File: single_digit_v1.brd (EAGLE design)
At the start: 101.6 x 50.8 mm, 85 parts

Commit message: ready for production
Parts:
- added R43, R44, R45: (no value), rcl:M0805
- added SL1: (no value), con-amp-quick:02P
- added T8, T9: (no value), transistor:SOT23-BEC
- T1, T2, T3, T4, T5, T6, T7: device transistor-neu-to92:TO92-EBC -> transistor:SOT23-BEC
- moved T2 9.17 mm to (83.8, 17.5), turned to 270 degrees
- moved R37 8.48 mm to (63.5, 36.8), turned to 135 degrees
- moved T3 7.44 mm to (69.5, 36.2), turned to 0 degrees
- moved T7 6.17 mm to (19.2, 16.0), turned to 180 degrees
- moved T4 5.88 mm to (73.0, 15.2), turned to 180 degrees
- moved R36 5.86 mm to (78.2, 18.5), turned to 180 degrees
- moved R41 4.73 mm to (25.8, 16.5)
- moved R42 4.59 mm to (16.0, 26.2)
- moved JP1 4.39 mm to (35.0, 25.0), turned to 270 degrees
- moved R39 4.05 mm to (62.8, 26.5)
- moved T1 3.83 mm to (15.0, 21.5), turned to 90 degrees
- moved T5 3.46 mm to (61.2, 21.5), turned to 90 degrees
- moved R38 3.38 mm to (67.8, 16.2)
- moved R40 2.23 mm to (28.2, 34.2)
- moved T6 2.21 mm to (22.8, 36.5), turned to 0 degrees
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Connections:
- new net N$50: R43.2, T8.C
- new net N$51: R43.1, R44.2, T9.B
- new net N$52: R45.1, T8.B
- new net N$53: R45.2, SL1.1
- new net VCC: LED1.A, LED10.A, LED11.A, LED12.A, LED13.A, LED14.A, LED15.A, LED16.A, LED17.A, LED18.A, LED19.A, LED2.A, LED20.A, LED21.A, LED22.A, LED23.A, LED24.A, LED25.A, LED26.A, LED27.A, LED28.A, LED29.A, LED3.A, LED30.A, LED31.A, LED32.A, LED33.A, LED34.A, LED35.A, LED4.A, LED5.A, LED6.A, LED7.A, LED8.A, LED9.A, T9.C
- net +5V: now also R44.1, SL1.2, T9.E; no longer JP1.5, LED1.A, LED10.A, LED11.A, LED12.A, LED13.A, LED14.A, LED15.A, LED16.A, LED17.A, LED18.A, LED19.A, LED2.A, LED20.A, LED21.A, LED22.A, LED23.A, LED24.A, LED25.A, LED26.A, LED27.A, LED28.A, LED29.A, LED3.A, LED30.A, LED31.A, LED32.A, LED33.A, LED34.A, LED35.A, LED4.A, LED5.A, LED6.A, LED7.A, LED8.A, LED9.A
- net GNDA: now also JP1.5, JP1.8, T8.E
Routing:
- net +5V: track 378.9 -> 16.7 mm
- net VCC: track 0.00 -> 55.7 mm, vias 0 -> 1
- net GNDA: track 0.00 -> 12.1 mm
- net S6: track 6.72 -> 18.4 mm
- net S7: track 22.6 -> 33.1 mm
- net N$51: track 0.00 -> 9.72 mm
- net S1: track 65.7 -> 74.7 mm, vias 2 -> 0
- net S5: track 6.72 -> 13.8 mm
- net N$50: track 0.00 -> 7.00 mm
- net S4: track 43.7 -> 50.6 mm
- net N$49: track 4.13 -> 9.31 mm
- net S3: track 48.0 -> 52.5 mm, vias 2 -> 0
- net N$53: track 0.00 -> 4.31 mm
- net N$52: track 0.00 -> 3.43 mm
- net N$42: track 4.13 -> 7.23 mm
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- added copper zone on layer 16, net VCC
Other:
- board size 101.6 x 50.8 mm -> 100 x 50 mm
- board text added: "+"

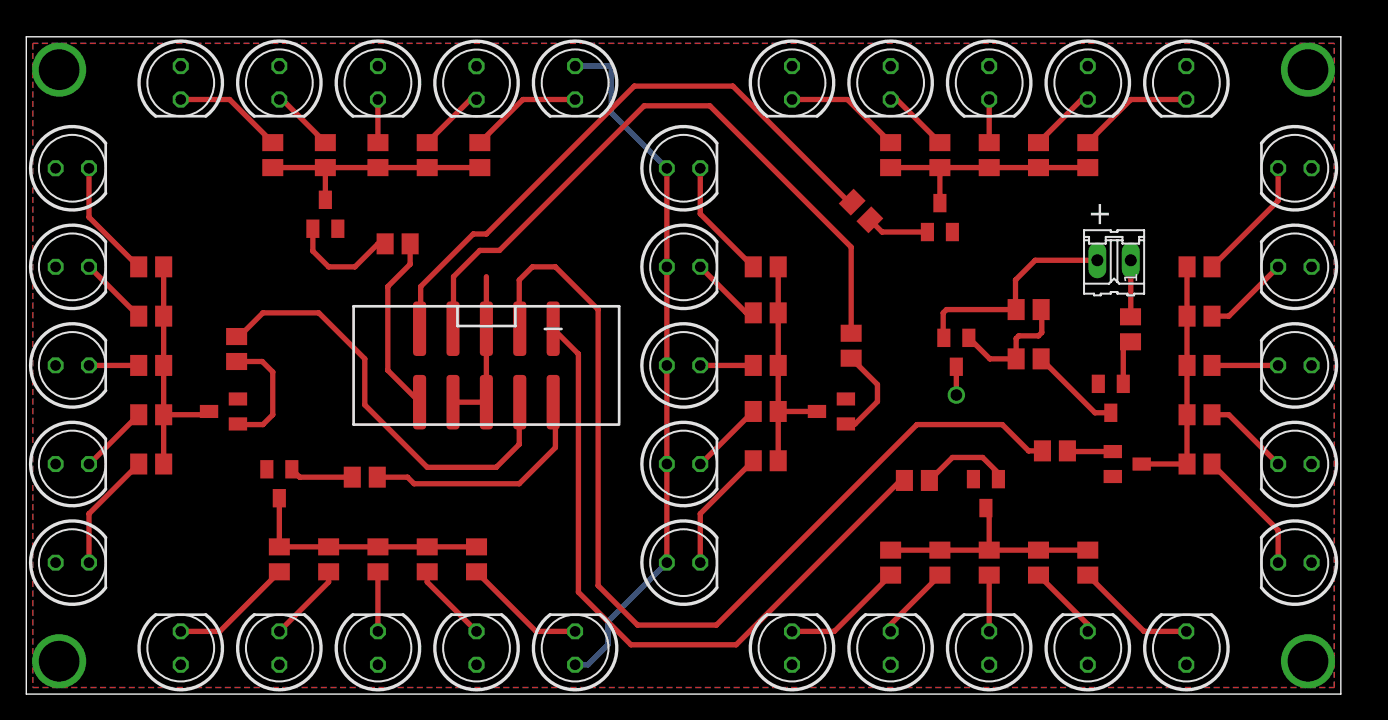
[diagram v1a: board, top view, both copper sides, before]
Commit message: add labels to boards to aid in, you know, using them
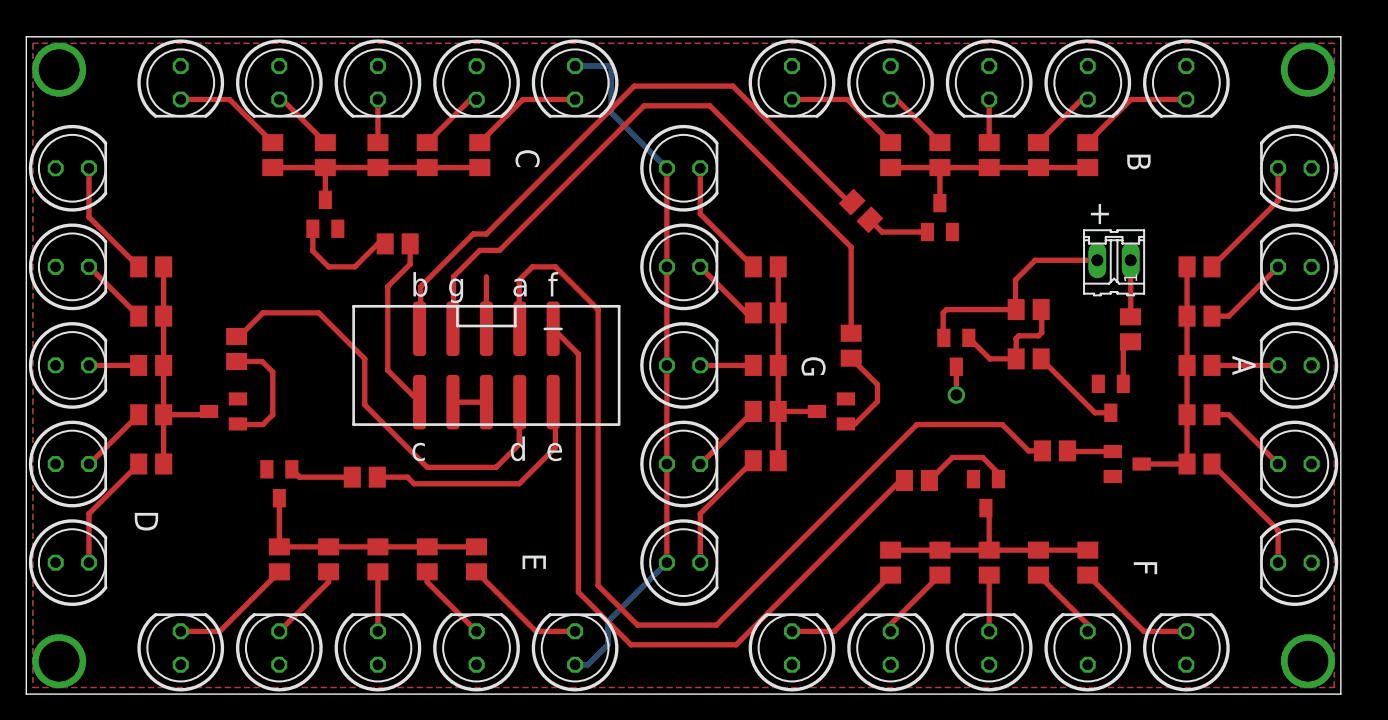
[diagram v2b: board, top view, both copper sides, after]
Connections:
- net S1 renamed SEG_A
- net S2 renamed SEG_B
- net S3 renamed SEG_F
- net S4 renamed SEG_G
- net S5 renamed SEG_C
- net S6 renamed SEG_E
- net S7 renamed SEG_D
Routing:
- net GNDA: track 12.1 -> 6.50 mm
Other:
- board text added: "A"
- board text added: "B"
- board text added: "C"
- board text added: "D"
- board text added: "E"
- board text added: "F"
- board text added: "G"
- board text added: "b g a f"
- board text added: "c d e"
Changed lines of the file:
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@@
 <wire x1="0" y1="50" x2="0" y2="0" width="0" layer="20"/>
 <text x="80.75" y="35.75" size="1.778" layer="25">+</text>
+<text x="29.25" y="30.25" size="1.778" layer="25">b  g     a  f</text>
+<text x="29.25" y="17.75" size="1.778" layer="25">c         d  e</text>
+<text x="91.75" y="25.75" size="1.778" layer="25" rot="SR270">A</text>
+<text x="83.75" y="41.25" size="1.778" layer="25" rot="SR270">B</text>
+<text x="37.25" y="41.5" size="1.778" layer="25" rot="SR270">C</text>
+<text x="8.25" y="14" size="1.778" layer="25" rot="SR270">D</text>
+<text x="37.75" y="10.75" size="1.778" layer="25" rot="SR270">E</text>
+<text x="84.25" y="10.25" size="1.778" layer="25" rot="SR270">F</text>
+<text x="59" y="25.75" size="1.778" layer="25" rot="SR270">G</text>
 </plain>
 <attributes>
@@
 <contactref element="T7" pad="E"/>
 <contactref element="T1" pad="E"/>
-<contactref element="JP1" pad="6"/>
 <contactref element="T8" pad="E"/>
-<contactref element="JP1" pad="8"/>
 <contactref element="JP1" pad="5"/>
 <polygon width="0.4064" layer="1" isolate="0.381">
@@
 </polygon>
 <wire x1="35" y1="27.794" x2="35" y2="31.75" width="0.4064" layer="1"/>
-<wire x1="35" y1="27.794" x2="35" y2="22.206" width="0.4064" layer="1"/>
+<contactref element="JP1" pad="6"/>
+<contactref element="JP1" pad="8"/>
 <wire x1="32.46" y1="22.206" x2="35" y2="22.206" width="0.4064" layer="1"/>
 </signal>
@@
 <wire x1="16.15" y1="20.5" x2="16.1" y2="20.55" width="0.4064" layer="1"/>
 </signal>
-<signal name="S2">
+<signal name="SEG_B">
 <contactref element="R37" pad="2"/>
 <contactref element="JP1" pad="9"/>
@@
 <wire x1="30" y1="27.874" x2="29.92" y2="27.794" width="0.4064" layer="1"/>
 </signal>
-<signal name="S3">
+<signal name="SEG_F">
 <contactref element="JP1" pad="1"/>
 <contactref element="R38" pad="2"/>
@@
 <wire x1="42" y1="25.874" x2="40.08" y2="27.794" width="0.4064" layer="1"/>
 </signal>
-<signal name="S4">
-<contactref element="R39" pad="2"/>
-<contactref element="JP1" pad="7"/>
-<wire x1="62.75" y1="27.45" x2="62.75" y2="34" width="0.4064" layer="1"/>
-<wire x1="62.75" y1="34" x2="52" y2="44.75" width="0.4064" layer="1"/>
-<wire x1="52" y1="44.75" x2="47" y2="44.75" width="0.4064" layer="1"/>
-<wire x1="47" y1="44.75" x2="36" y2="33.75" width="0.4064" layer="1"/>
-<wire x1="36" y1="33.75" x2="34.5" y2="33.75" width="0.4064" layer="1"/>
-<wire x1="34.5" y1="33.75" x2="32.5" y2="31.75" width="0.4064" layer="1"/>
-<wire x1="32.5" y1="31.75" x2="32.5" y2="27.834" width="0.4064" layer="1"/>
-<wire x1="32.5" y1="27.834" x2="32.46" y2="27.794" width="0.4064" layer="1"/>
-</signal>
-<signal name="S1">
+<signal name="SEG_A">
 <contactref element="R36" pad="2"/>
 <contactref element="JP1" pad="3"/>
@@
 <wire x1="76.25" y1="18.5" x2="77.3" y2="18.5" width="0.4064" layer="1"/>
 </signal>
-<signal name="S7">
-<contactref element="R42" pad="2"/>
-<contactref element="JP1" pad="4"/>
-<wire x1="25.75" y1="25.5" x2="25.75" y2="22" width="0.4064" layer="1"/>
-<wire x1="25.75" y1="22" x2="30.5" y2="17.25" width="0.4064" layer="1"/>
-<wire x1="30.5" y1="17.25" x2="35.75" y2="17.25" width="0.4064" layer="1"/>
-<wire x1="35.75" y1="17.25" x2="37.5" y2="19" width="0.4064" layer="1"/>
-<wire x1="37.5" y1="19" x2="37.5" y2="22.166" width="0.4064" layer="1"/>
-<wire x1="37.5" y1="22.166" x2="37.54" y2="22.206" width="0.4064" layer="1"/>
-<wire x1="25.75" y1="25.5" x2="22.25" y2="29" width="0.4064" layer="1"/>
-<wire x1="22.25" y1="29" x2="18" y2="29" width="0.4064" layer="1"/>
-<wire x1="18" y1="29" x2="16.2" y2="27.2" width="0.4064" layer="1"/>
-<wire x1="16.2" y1="27.2" x2="16" y2="27.2" width="0.4064" layer="1"/>
-</signal>
-<signal name="S5">
-<contactref element="R40" pad="2"/>
-<contactref element="JP1" pad="10"/>
-<wire x1="29.2" y1="34.25" x2="29.2" y2="32.7" width="0.4064" layer="1"/>
-<wire x1="29.2" y1="32.7" x2="27.5" y2="31" width="0.4064" layer="1"/>
-<wire x1="27.5" y1="31" x2="27.5" y2="24.626" width="0.4064" layer="1"/>
-<wire x1="27.5" y1="24.626" x2="29.92" y2="22.206" width="0.4064" layer="1"/>
-</signal>
-<signal name="S6">
+<signal name="SEG_E">
 <contactref element="R41" pad="2"/>
 <contactref element="JP1" pad="2"/>
@@
 <via x="2.5" y="2.5" extent="1-16" drill="3.1"/>
 </signal>
+<signal name="SEG_C">
+<contactref element="R40" pad="2"/>
+<contactref element="JP1" pad="10"/>
+<wire x1="29.2" y1="32.7" x2="27.5" y2="31" width="0.4064" layer="1"/>
+<wire x1="27.5" y1="31" x2="27.5" y2="24.626" width="0.4064" layer="1"/>
+<wire x1="27.5" y1="24.626" x2="29.92" y2="22.206" width="0.4064" layer="1"/>
+<wire x1="29.2" y1="32.7" x2="29.2" y2="34.25" width="0.4064" layer="1"/>
+</signal>
+<signal name="SEG_D">
+<contactref element="R42" pad="2"/>
+<contactref element="JP1" pad="4"/>
+<wire x1="25.75" y1="25.5" x2="25.75" y2="22" width="0.4064" layer="1"/>
+<wire x1="25.75" y1="22" x2="30.5" y2="17.25" width="0.4064" layer="1"/>
+<wire x1="30.5" y1="17.25" x2="35.75" y2="17.25" width="0.4064" layer="1"/>
+<wire x1="35.75" y1="17.25" x2="37.5" y2="19" width="0.4064" layer="1"/>
+<wire x1="37.5" y1="19" x2="37.5" y2="22.166" width="0.4064" layer="1"/>
+<wire x1="37.5" y1="22.166" x2="37.54" y2="22.206" width="0.4064" layer="1"/>
+<wire x1="25.75" y1="25.5" x2="22.25" y2="29" width="0.4064" layer="1"/>
+<wire x1="22.25" y1="29" x2="18" y2="29" width="0.4064" layer="1"/>
+<wire x1="18" y1="29" x2="16.2" y2="27.2" width="0.4064" layer="1"/>
+<wire x1="16.2" y1="27.2" x2="16" y2="27.2" width="0" layer="19" extent="1-1"/>
+</signal>
+<signal name="SEG_G">
+<contactref element="R39" pad="2"/>
+<contactref element="JP1" pad="7"/>
+<wire x1="62.75" y1="34" x2="52" y2="44.75" width="0.4064" layer="1"/>
+<wire x1="52" y1="44.75" x2="47" y2="44.75" width="0.4064" layer="1"/>
+<wire x1="47" y1="44.75" x2="36" y2="33.75" width="0.4064" layer="1"/>
+<wire x1="36" y1="33.75" x2="34.5" y2="33.75" width="0.4064" layer="1"/>
+<wire x1="34.5" y1="33.75" x2="32.5" y2="31.75" width="0.4064" layer="1"/>
+<wire x1="32.5" y1="31.75" x2="32.5" y2="27.834" width="0.4064" layer="1"/>
+<wire x1="32.5" y1="27.834" x2="32.46" y2="27.794" width="0.4064" layer="1"/>
+<wire x1="62.75" y1="27.45" x2="62.75" y2="34" width="0.4064" layer="1"/>
+</signal>
 </signals>
